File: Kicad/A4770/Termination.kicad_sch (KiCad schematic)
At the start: 29 parts, among them J1 5749721-7, J2 5787082-7, J3 TO-LED, J4 TO-MB, J5 TO-A3000-LED, J6 TO-A3000-MB, U10 DS21S07A, U11 DS21S07A, U12 DS21S07A

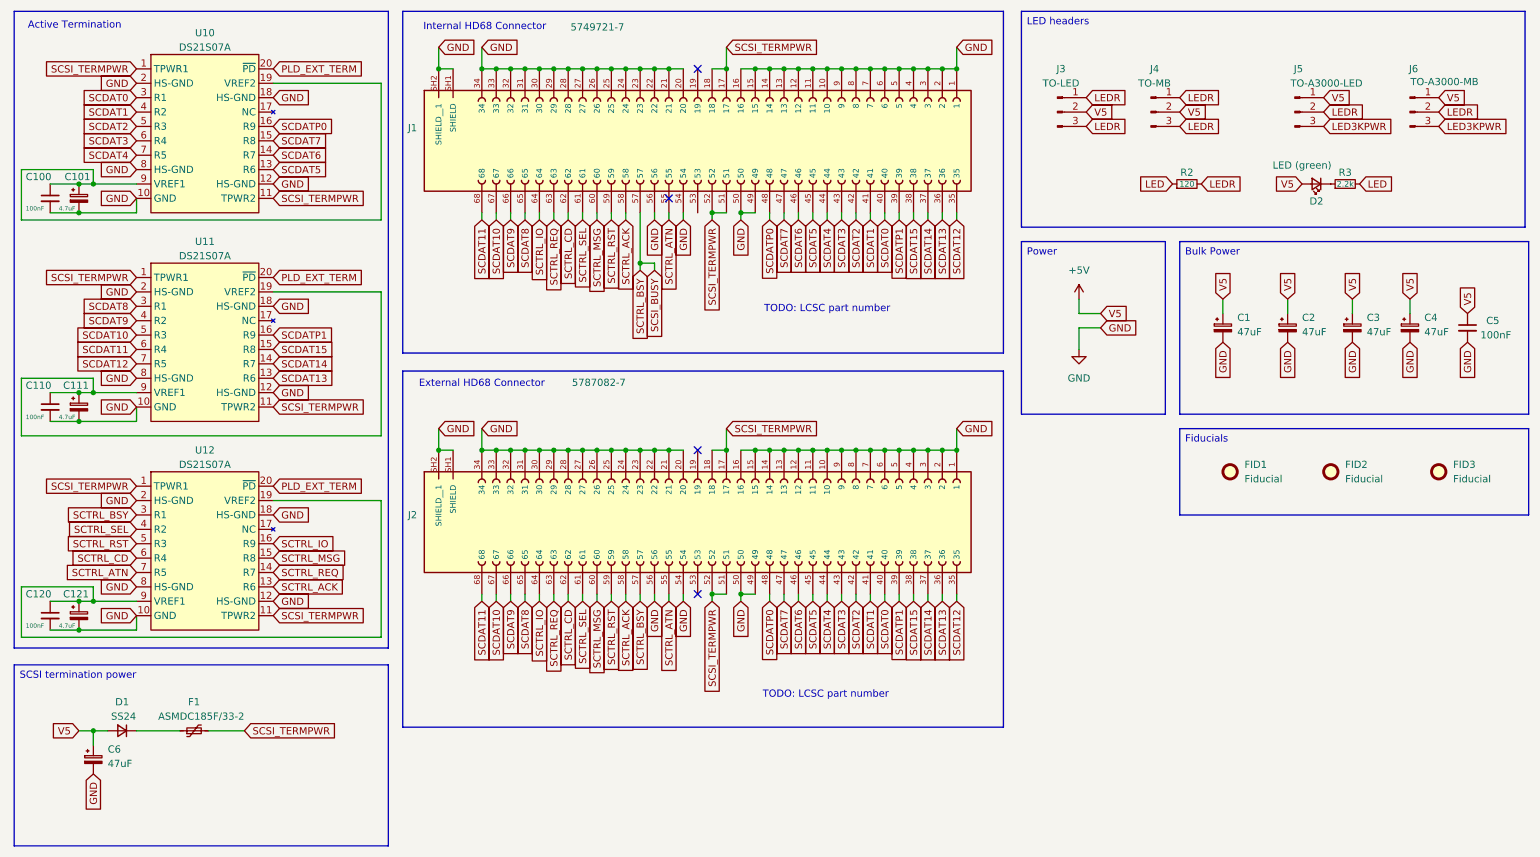
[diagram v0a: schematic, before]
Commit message: Changes from schematics review 26-02-08
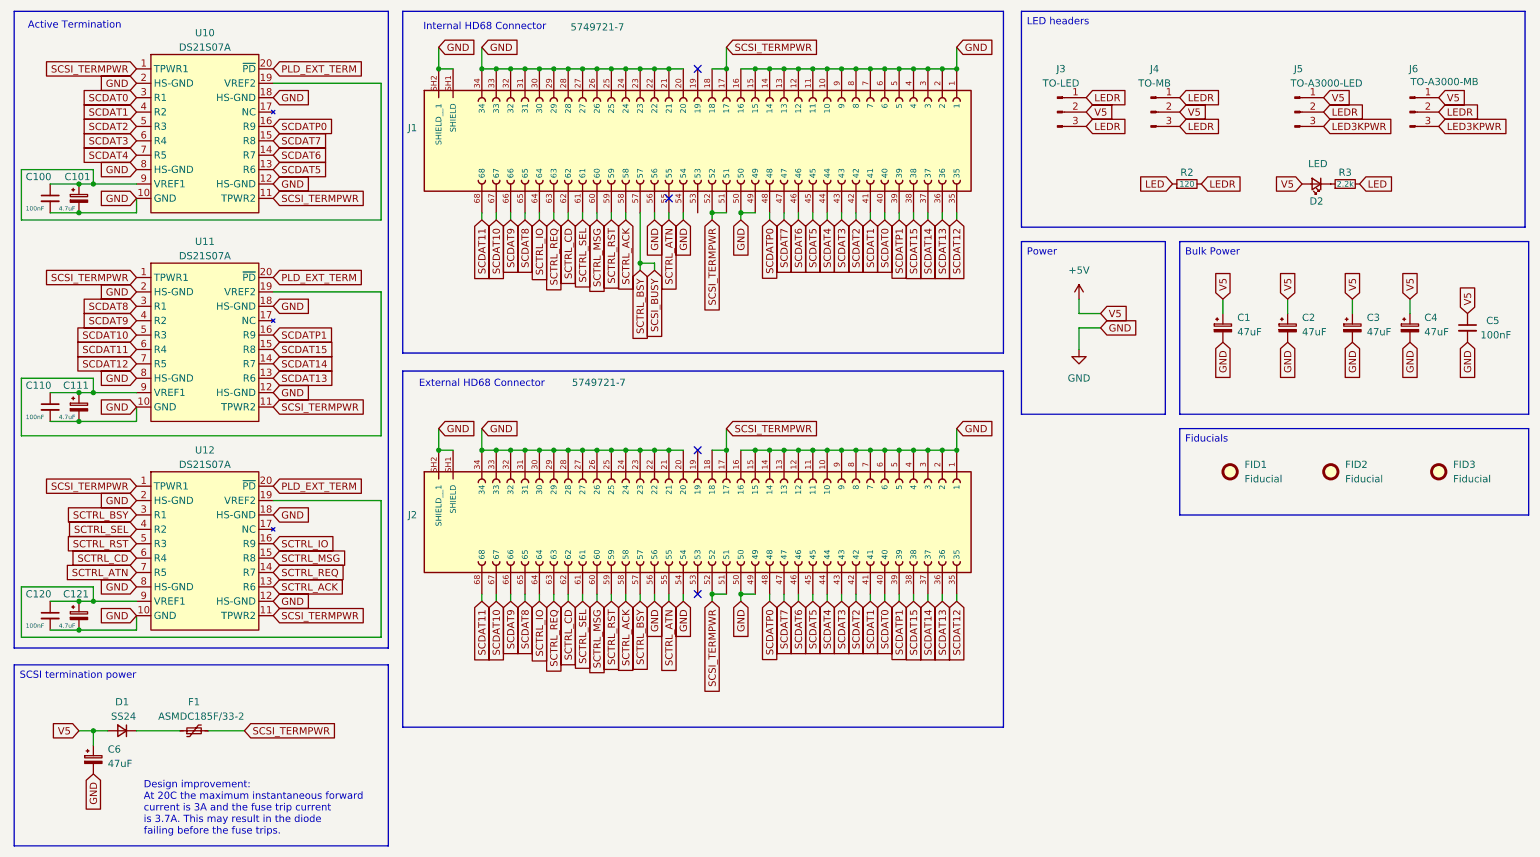
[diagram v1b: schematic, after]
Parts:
- D2: value LED (green) -> LED
- J2: value 5787082-7 -> 5749721-7
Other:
- note added: "Design improvement: At 20C the maximum instantaneous forward current is 3A and the fuse trip current is 3.7A. This may result in the diode failing before the fuse trips."
- note removed: "TODO: LCSC part number"
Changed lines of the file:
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@@
 		)
 	)
-	(text "TODO: LCSC part number"
-		(exclude_from_sim no)
-		(at 158.496 135.89 0)
-		(effects
-			(font
-				(size 1.27 1.27)
-			)
-		)
-	)
 	(text "Active Termination\n"
 		(exclude_from_sim no)
@@
 		)
 	)
-	(text "TODO: LCSC part number"
+	(text "Design improvement:\nAt 20C the maximum instantaneous forward\ncurrent is 3A and the fuse trip current \nis 3.7A. This may result in the diode \nfailing before the fuse trips."
 		(exclude_from_sim no)
-		(at 158.75 67.818 0)
+		(at 38.1 155.956 0)
 		(effects
 			(font
 				(size 1.27 1.27)
 			)
+			(justify left)
 		)
 	)
@@
 			)
 		)
-		(property "Value" "5787082-7"
+		(property "Value" "5749721-7"
 			(at 123.19 80.772 90)
 			(effects
@@
 			)
 		)
-		(property "Value" "LED (green)"
-			(at 242.57 42.418 0)
+		(property "Value" "LED"
+			(at 245.364 42.164 0)
 			(effects
 				(font

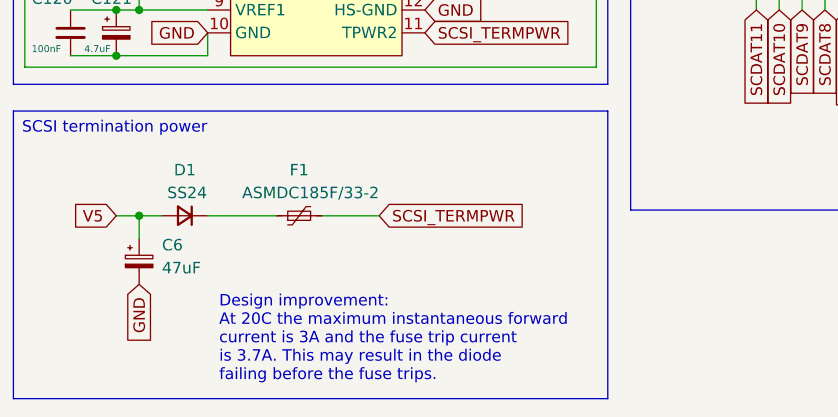
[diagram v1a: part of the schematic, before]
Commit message: Update TERMPWR diode to DSS34
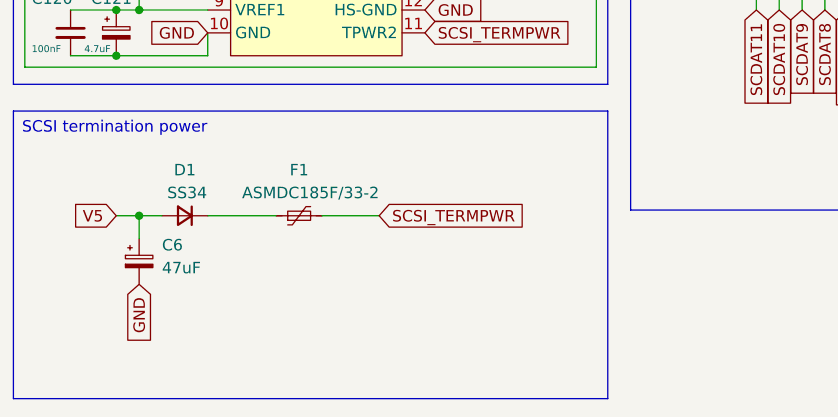
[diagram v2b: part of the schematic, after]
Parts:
- D1: value SS24 -> SS34; LCSC Part # C43381 -> C466483
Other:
- note removed: "Design improvement: At 20C the maximum instantaneous forward current is 3A and the fuse trip current is 3.7A. This may result in the diode failing before the fuse trips."
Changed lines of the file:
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@@
 		)
 	)
-	(text "Design improvement:\nAt 20C the maximum instantaneous forward\ncurrent is 3A and the fuse trip current \nis 3.7A. This may result in the diode \nfailing before the fuse trips."
-		(exclude_from_sim no)
-		(at 38.1 155.956 0)
-		(effects
-			(font
-				(size 1.27 1.27)
-			)
-			(justify left)
-		)
-	)
 	(text_box "SCSI termination power\n"
 		(exclude_from_sim no)
@@
 			)
 		)
-		(property "Value" "SS24"
+		(property "Value" "SS34"
 			(at 34.544 139.7 0)
 			(effects
@@
 			)
 		)
-		(property "Datasheet" "https://www.onsemi.com/pdf/datasheet/mbr140sft1-d.pdf"
+		(property "Datasheet" "https://www.lcsc.com/datasheet/C466483.pdf"
 			(at 34.29 142.24 90)
 			(effects
@@
 			)
 		)
-		(property "LCSC Part #" "C43381"
+		(property "LCSC Part #" "C466483"
 			(at 34.29 142.24 0)
 			(effects

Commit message: Fix up part numbers
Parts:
- F1: LCSC Alt # C780180 -> C3761950; LCSC Alt 2 # (none) -> C135379; LCSC Part # C135379 -> C780180
- J2: LCSC Part # C591676 -> C591675
